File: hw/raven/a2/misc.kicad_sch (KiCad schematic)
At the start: 71 parts, among them J601 TRSx2, J602 PinHdr_01x04, J603 PinHdr_01x04, J604 PinHdr_01x04, J605 Pinhdr_01x02, J606 DB25/9/9, J607 PinHdr_01x04, J608 DB9M/9M, J609 USB+Ethernet, U601 MCP4251, U602 PAM8302AAD, U603 CNY17F-3, U604 74LS07

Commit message: A2: DAC for DSP and mix with YM
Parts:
- added C613, C614: 2.2n, Capacitor_SMD:C_1206_3216Metric_Pad1.33x1.80mm_HandSolder, symbol 68k:c_100nf_smd1206
- added R618, R619, R620, R621: 10K, Resistor_SMD:R_1206_3216Metric_Pad1.30x1.75mm_HandSolder, symbol Device:R
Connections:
- net AUDIO_YM_L: now also R618.2; no longer J603.4 (Pin_4), R612.2
- net AUDIO_YM_R: now also R620.2; no longer J603.1 (Pin_1), R611.2
- net GND: now also C613.2, C614.1
- net AUDIO_YM_RAW_L: now reaches R601.1, R602.1, U601.8 (P0A)
- net AUDIO_YM_RAW_R: now reaches R603.1, R604.1, U601.7 (P1A)
- new net AUDIO_DSP_L: C613.1, R619.2
- new net AUDIO_DSP_R: C614.2, R621.2
- new net AUDIO_OUT_L: J603.4 (Pin_4), R612.2, R618.1, R619.1
- new net AUDIO_OUT_R: J603.1 (Pin_1), R611.2, R620.1, R621.1
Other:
- note added: "Line out"
- note added: "YM + DSP mix"
- note added: "YM stereo mix"
- note added: "YM volume"
- note removed: "cut2"
- moved on the sheet: C601, C602, C603, C604, C605, C606, C607, C608, C609, J601, J602, J603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

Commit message: A2: dac + adc + dsp work
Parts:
- renumbered C610 to C601, C611 to C602, C612 to C603, C601 to C604, C602 to C605, C614 to C606, C603 to C607, C604 to C608, C613 to C609, C605 to C610, C607 to C611, C606 to C612, C608 to C613, C609 to C614, J609 to J601, J606 to J602, J607 to J603, J608 to J604, J601 to J605, J602 to J606, J603 to J607, J604 to J608, J605 to J609, R614 to R601, R615 to R602, R616 to R603, R617 to R604, R620 to R605, R601 to R606, R621 to R607, R602 to R608, R603 to R609, R604 to R610, R605 to R611, R606 to R612, R607 to R613, R618 to R614, R619 to R615, R611 to R616, R608 to R617, R609 to R618, R610 to R619, R612 to R620, R613 to R621, U603 to U601, U604 to U602, U602 to U603, U601 to U604
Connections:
- net YM:CHA: now also C604.1; no longer C604.2
- net YM:CHB: now also C605.1, C607.1; no longer C605.2, C607.2
- net YM:CHC: now also C608.1; no longer C608.2
- net at R608.2: now also C605.2; no longer C605.1
- net at R606.2: now also C604.2; no longer C604.1
- net at R609.2: now also C607.2; no longer C607.1
- net at R610.2: now also C608.2; no longer C608.1
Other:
- note added: "shdn forces PxW to PxB can be controlled from software so no need for hardware pin."
- note added: "spkr_on"
- note added: "to dsp to pot->line"
- note added: "to line"
- note added: "to line to amp->spkr"
- note added: "vol_clk"
- note added: "vol_cs"
- note added: "vol_dta"
- note added: "wrong orientation"
- note removed: "cut1"
- moved on the sheet: C604, C605, C607, C608, R606, R608, R609, R610, R617, R618, R619

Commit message: misc a2 work
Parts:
- removed C602: 10u, Capacitor_SMD:C_1206_3216Metric_Pad1.33x1.80mm_HandSolder, symbol 68k:c_100nf_smd1206
- removed J601: USB+Ethernet, 68k:AMPHENOL_RJMG231022830ER, symbol 68k:RJMG231022830ER
- added J604: USB1035-GF-P-0-B-B, 68k:USB1035GFP0BB, symbol 68k:USB1035-GF-P-0-B-B
- J603: renamed from J604; footprint K42XE9PPA4NJ -> 68k:K42XE9PPA4NJ
- U601: footprint DIP762W60P254L730H430Q6N -> 68k:DIP762W60P254L730H430Q6N
- renumbered C603 to C602, C604 to C603, C605 to C604, C606 to C605, C607 to C606, C608 to C607, C609 to C608, C610 to C609, C611 to C610, C612 to C611, C613 to C612, C614 to C613, J602 to J601, J603 to J602
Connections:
- net GND: now also C601.2, J604.A4, J604.B4; no longer C601.1
- net MIDI_IN_T: no longer U601.3 (NC_1)
- net SHIELD: now also J604.1 (MH1), J604.2 (MH2), J604.3 (MH3), J604.4 (MH4)
- net USB0:D+: now also J604.B3
- net USB0:D-: now also J604.B2
- net USB1:D+: now also J604.A3
- net USB1:D-: now also J604.A2
- net VUSB: now also C601.1, J604.A1, J604.B1; no longer C601.2
- net COM1:CD: no longer names the net of J601.A1
- net COM1:DSR: no longer names the net of J601.A6
- net COM1:RI: no longer names the net of J601.A9
- no-connect marks 28 -> 31
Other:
- note removed: "Ethernet"
- note removed: "RJ1"
- note removed: "RJ2"
- note removed: "RJ3"
- note removed: "RJ4"
- note removed: "RJ5"
- note removed: "RJ6"
- note removed: "RJ7"
- note removed: "RJ8"
- note removed: "usb host"
- note removed: "usb host / device"
- moved on the sheet: C601, D601, R602

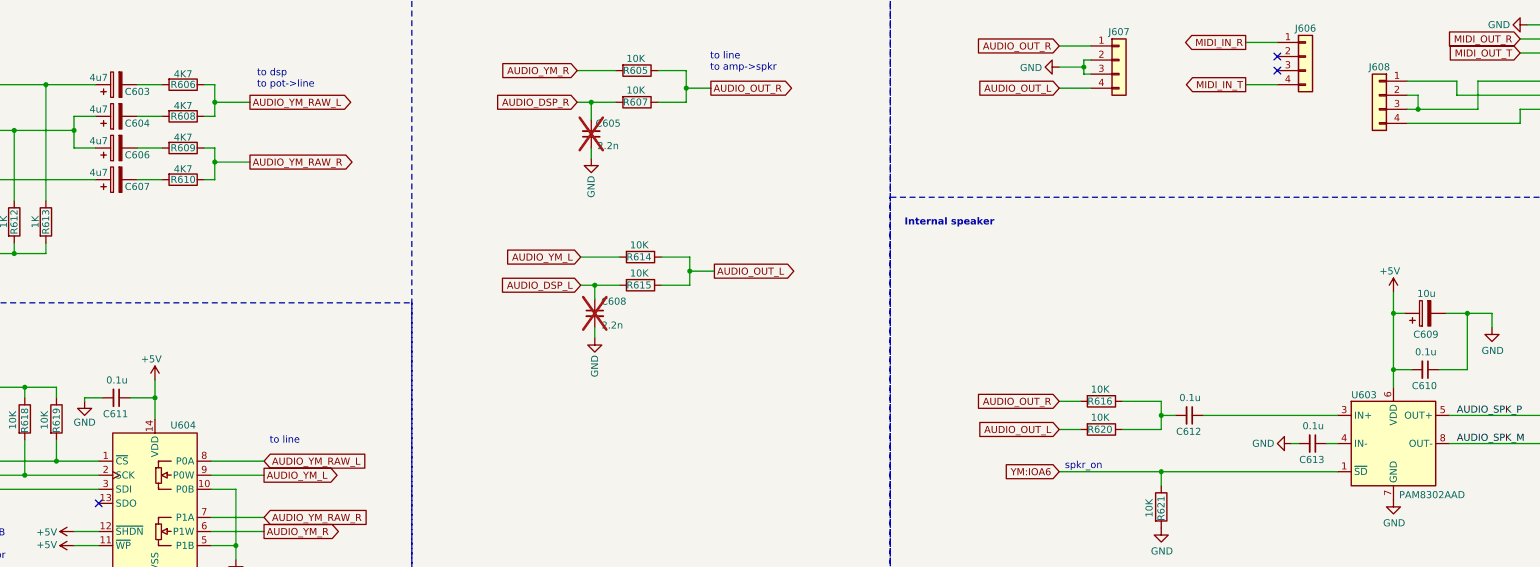
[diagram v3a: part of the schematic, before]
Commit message: A2: schema + routing complete. ERC + DRC complete.
Let sit for a while, revisit and sanity check with fresh eyes before gerber.
Todo: double check BOM export and fix missing infos if any.
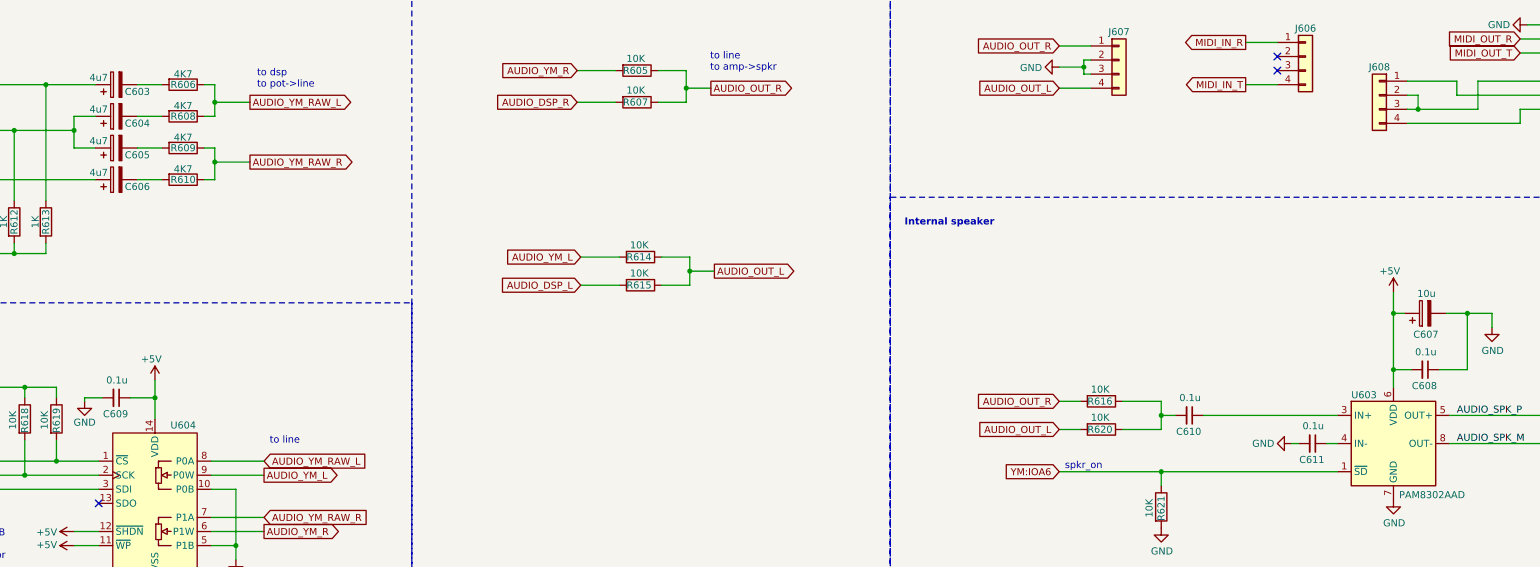
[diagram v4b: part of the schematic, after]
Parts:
- removed C605, C608: 2.2n, Capacitor_SMD:C_1206_3216Metric_Pad1.33x1.80mm_HandSolder, symbol 68k:c_100nf_smd1206
- renumbered C606 to C605, C607 to C606, C609 to C607, C610 to C608, C611 to C609, C612 to C610, C613 to C611

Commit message: cosmetic
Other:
- moved on the sheet: C602, C607, C608, C610, C611

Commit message: A2: cosmetics and bom preparations
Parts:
- C603, C604, C605, C606: footprint Capacitor_THT:CP_Radial_D5.0mm_P2.50mm -> Capacitor_THT:CP_Radial_D5.0mm_P2.00mm; Manufacturer_Part_Number EEU-EB1H4R7SH -> ECE-A1HKS4R7
- C607: footprint Capacitor_THT:CP_Radial_D5.0mm_P2.50mm -> Capacitor_THT:CP_Radial_D6.3mm_P2.50mm; Manufacturer_Part_Number EEU-EB1H100SH -> ECE-A1HKS100I
- J604: value USB1035-GF-P-0-B-B -> USBx2
- J609: value Pinhdr_01x02 -> PinHdr_01x02
- U602: Manufacturer_Name TI -> Texas Instruments
- U603: value PAM8302AAD -> PAM8302
- U604: Manufacturer_Name Microchip Technology -> Microchip

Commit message: A2: bom
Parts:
- C601: Manufacturer_Part_Number C1206C106K4RAC -> C1206C106K4RACTU
- JX611, JX612, JX613, JX614, JX615, JX616, JX617, JX618: Manufacturer_Name TE Connectivity -> Adam Tech; Manufacturer_Part_Number 1-881545-4 -> MSA-G
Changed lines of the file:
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@@
 			)
 		)
-		(property "Manufacturer_Name" "TE Connectivity"
+		(property "Manufacturer_Name" "Adam Tech"
 			(at 128.905 122.555 0)
 			(effects
@@
 			)
 		)
-		(property "Manufacturer_Part_Number" "1-881545-4"
+		(property "Manufacturer_Part_Number" "MSA-G"
 			(at 128.905 122.555 0)
 			(effects
@@
 			)
 		)
-		(property "Manufacturer_Name" "TE Connectivity"
+		(property "Manufacturer_Name" "Adam Tech"
 			(at 144.78 110.49 0)
 			(effects
@@
 			)
 		)
-		(property "Manufacturer_Part_Number" "1-881545-4"
+		(property "Manufacturer_Part_Number" "MSA-G"
 			(at 144.78 110.49 0)
 			(effects
@@
 			)
 		)
-		(property "Manufacturer_Name" "TE Connectivity"
+		(property "Manufacturer_Name" "Adam Tech"
 			(at 128.905 116.205 0)
 			(effects
@@
 			)
 		)
-		(property "Manufacturer_Part_Number" "1-881545-4"
+		(property "Manufacturer_Part_Number" "MSA-G"
 			(at 128.905 116.205 0)
 			(effects
@@
 			)
 		)
-		(property "Manufacturer_Part_Number" " C1206C106K4RAC"
+		(property "Manufacturer_Part_Number" " C1206C106K4RACTU"
 			(at 86.36 202.565 0)
 			(effects
@@
 			)
 		)
-		(property "Manufacturer_Name" "TE Connectivity"
+		(property "Manufacturer_Name" "Adam Tech"
 			(at 128.905 110.49 0)
 			(effects
@@
 			)
 		)
-		(property "Manufacturer_Part_Number" "1-881545-4"
+		(property "Manufacturer_Part_Number" "MSA-G"
 			(at 128.905 110.49 0)
 			(effects
@@
 			)
 		)
-		(property "Manufacturer_Name" "TE Connectivity"
+		(property "Manufacturer_Name" "Adam Tech"
 			(at 144.78 128.905 0)
 			(effects
@@
 			)
 		)
-		(property "Manufacturer_Part_Number" "1-881545-4"
+		(property "Manufacturer_Part_Number" "MSA-G"
 			(at 144.78 128.905 0)
 			(effects
@@
 			)
 		)
-		(property "Manufacturer_Name" "TE Connectivity"
+		(property "Manufacturer_Name" "Adam Tech"
 			(at 144.78 116.205 0)
 			(effects
@@
 			)
 		)
-		(property "Manufacturer_Part_Number" "1-881545-4"
+		(property "Manufacturer_Part_Number" "MSA-G"
 			(at 144.78 116.205 0)
 			(effects
@@
 			)
 		)
-		(property "Manufacturer_Name" "TE Connectivity"
+		(property "Manufacturer_Name" "Adam Tech"
 			(at 128.905 128.905 0)
 			(effects
@@
 			)
 		)
-		(property "Manufacturer_Part_Number" "1-881545-4"
+		(property "Manufacturer_Part_Number" "MSA-G"
 			(at 128.905 128.905 0)
 			(effects
@@
 			)
 		)
-		(property "Manufacturer_Name" "TE Connectivity"
+		(property "Manufacturer_Name" "Adam Tech"
 			(at 144.78 122.555 0)
 			(effects
@@
 			)
 		)
-		(property "Manufacturer_Part_Number" "1-881545-4"
+		(property "Manufacturer_Part_Number" "MSA-G"
 			(at 144.78 122.555 0)
 			(effects

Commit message: A2: minor clarifications
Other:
- note added: "unused"
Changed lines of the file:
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@@
+		)
+	)
+	(text "unused"
+		(exclude_from_sim no)
+		(at 188.722 197.612 0)
+		(effects
+			(font
+				(size 1.27 1.27)
+			)
 		)
 	)
